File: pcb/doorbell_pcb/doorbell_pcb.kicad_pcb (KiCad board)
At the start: 2 copper layers, 50 x 75 mm, 23 parts, among them J1 Conn_01x02_Socket, J2 Conn_01x02_Socket, J3 Conn_01x02_Pin, J4 Conn_01x03_Pin, SW1 SW_SPDT, U1 ACS712xLCTR-05B, U2 AMS1117-5.0

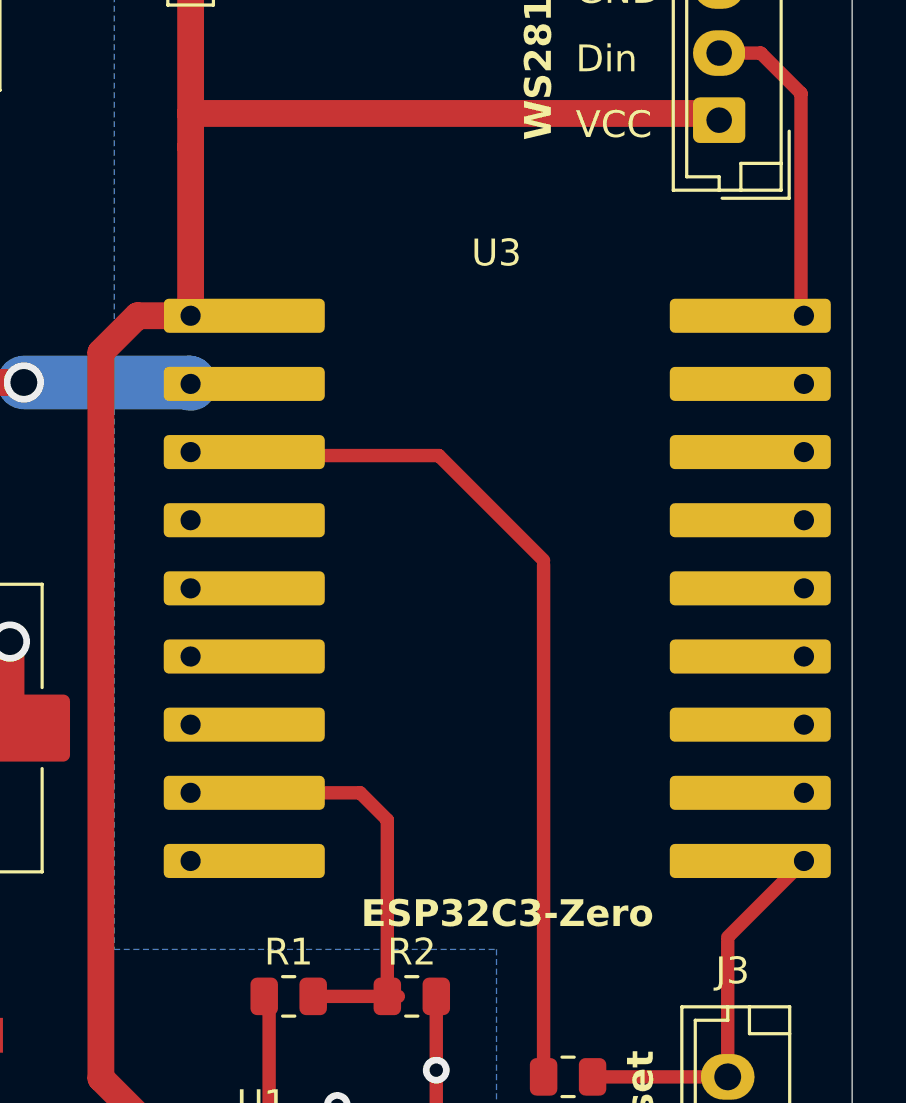
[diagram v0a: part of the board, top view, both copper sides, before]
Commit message: Update reset_page to use AbortController
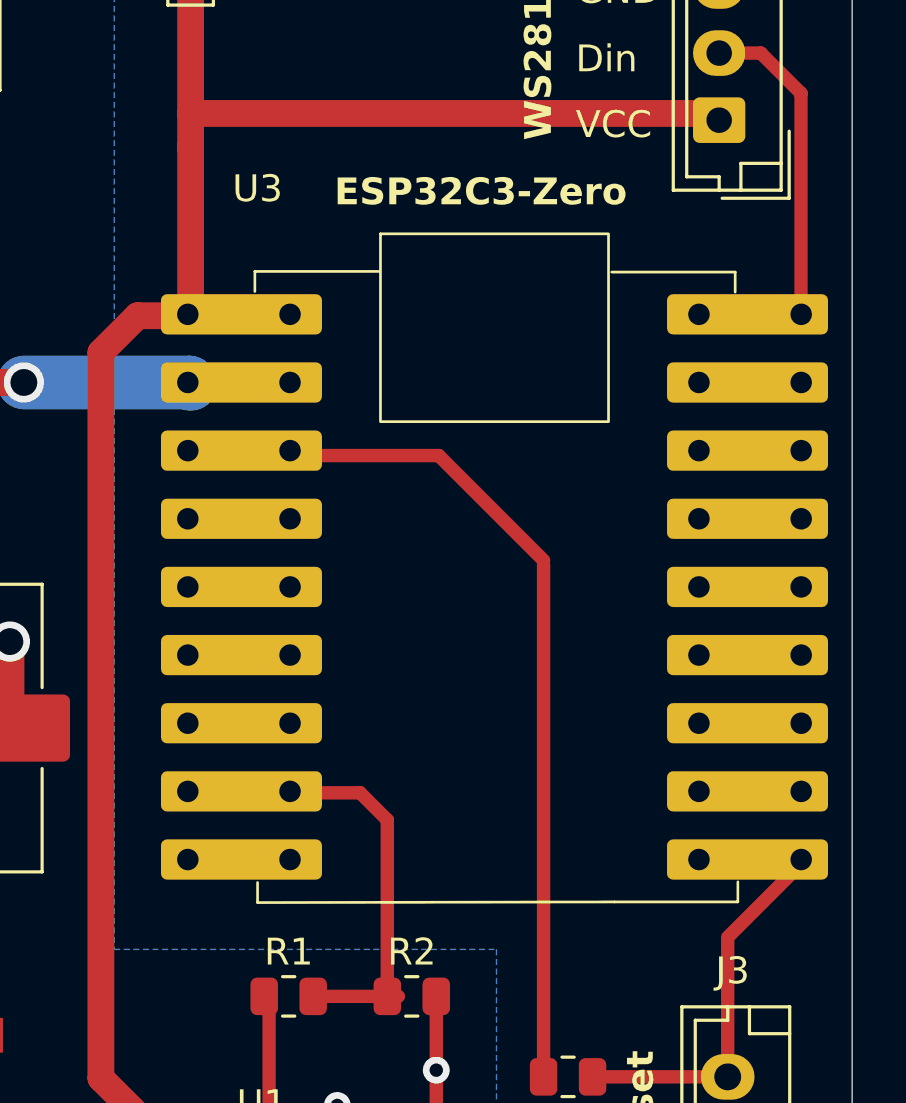
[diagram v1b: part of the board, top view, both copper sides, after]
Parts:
- moved U3 11.8 mm to (139.5, 87.6)
